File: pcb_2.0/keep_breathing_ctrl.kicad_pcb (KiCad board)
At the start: 4 copper layers, 153 x 148 mm, 260 parts, among them J1 Conn_02x04_Odd_Even, J2 1757284, J3 Conn_02x11_Odd_Even, P1 CONN_RASPBERRY, P2 Conn_01x04_Female, Q1 PN2222, Q2 PN2222, Q3 DMG2305UX, Q4 BCM857BS, Q5 2SC3325-Y, Q6 PN2222, Q7 PN2222, SW1 SW_DIP_x01, U1 MPL3115A2, U10 PCF8523TK, U11 AQH3223AX, U12 AQH3223AX, U13 HTS221, U14 ICE40UP5K-SG48ITR, U15 GD25Q32CTIGR-Memory_Flash, U16 UCC12040, U17 ISO7762, U18 XCL206B123, U19 AQH3223AX, U2 powerSTEP01, U20 AQH3223AX, U3 TLP240D, U4 TLP240D, U5 TLP240D, U6 TLP240D, U7 TLP240D, U8 TLP240D, U9 XCL214B333, X1 ABM8G, Y1 ABS06-107-32.768KHZ-T

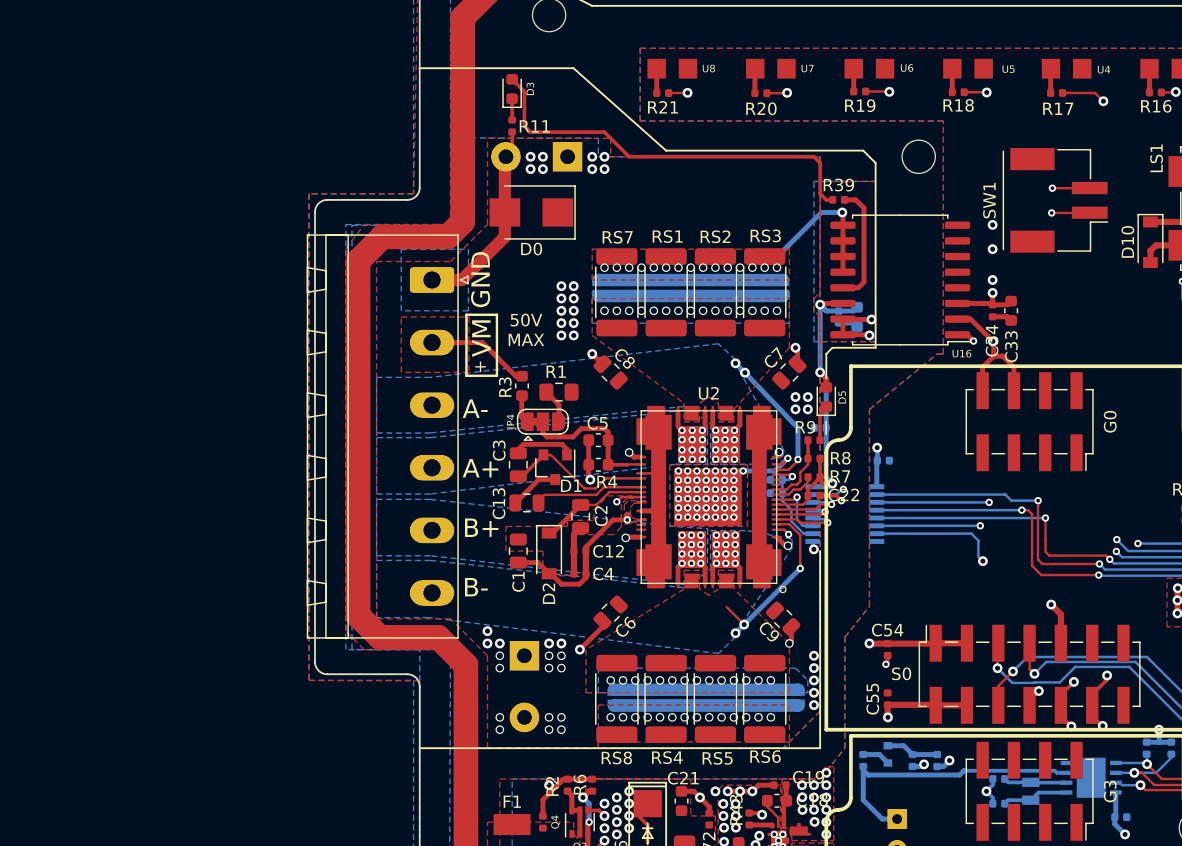
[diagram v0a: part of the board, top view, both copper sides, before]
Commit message: driver for motor eliminated
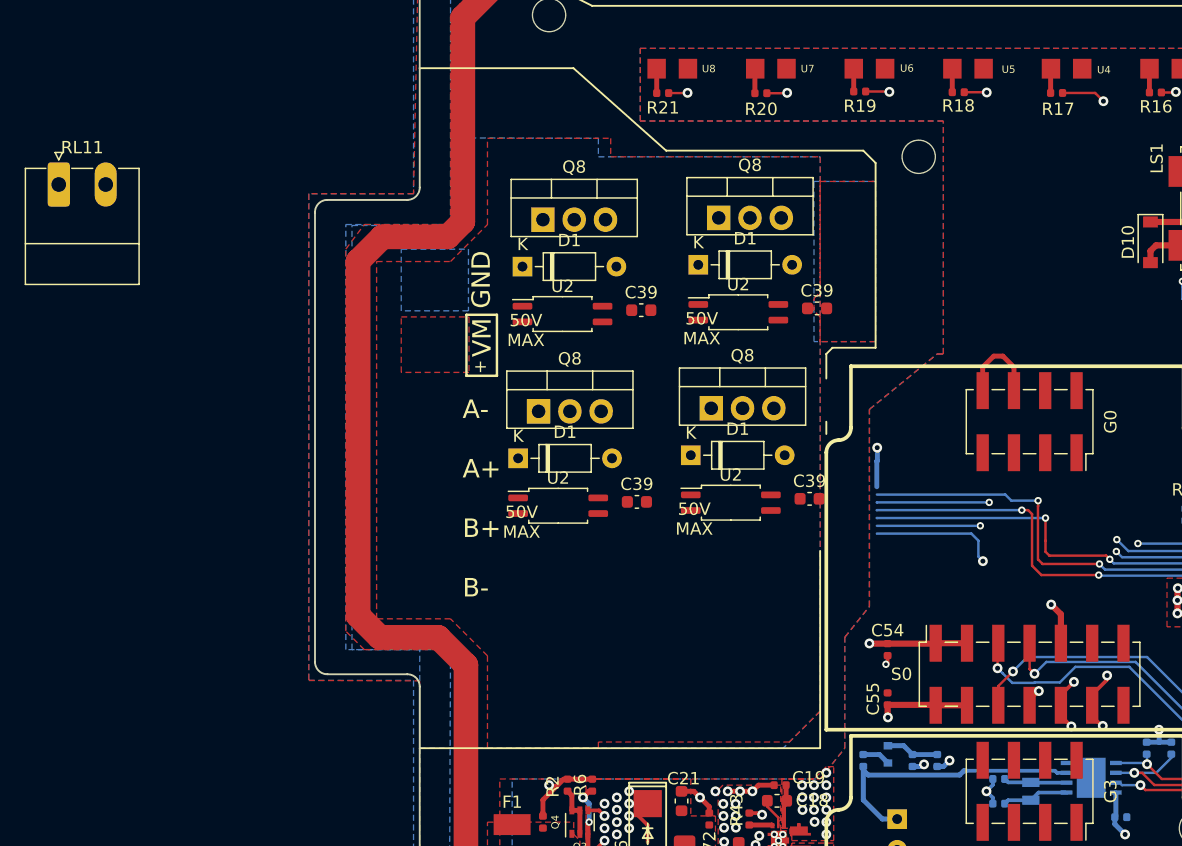
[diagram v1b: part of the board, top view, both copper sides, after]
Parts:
- removed C1: 22uF, Capacitor_SMD:C_0805_2012Metric
- removed C10, C11: 100uF 100V (Low ESR), Capacitor_THT:CP_Radial_D12.5mm_P5.00mm
- removed C12, C14, C22, C34, C35, C37, C74: 0.1uF, Capacitor_SMD:C_0402_1005Metric
- removed C13: 47nF 100V, Capacitor_SMD:C_0805_2012Metric
- removed C2, C3: 470nF 100V, Capacitor_SMD:C_0805_2012Metric
- removed C33, C36: 10uF, Capacitor_SMD:C_0603_1608Metric
- removed C4: 220nF, Capacitor_SMD:C_0402_1005Metric
- removed C5: 0.1uF, Capacitor_SMD:C_0603_1608Metric
- removed C6, C7, C8, C9: 220nF 100V, Capacitor_SMD:C_0805_2012Metric
- removed D0: 80V (Back EMF Clamp), Diode_SMD:D_SMB
- removed the D1 at (59.5, 87.7)
- removed D2: D_Schottky, Diode_SMD:D_SOD-123
- removed D3: LED GRN, Diode_SMD:D_0603_1608Metric
- removed D5: LED RED, Diode_SMD:D_0603_1608Metric
- removed J2: 1757284, Connector_Phoenix_MSTB:PhoenixContact_MSTBA_2,5_6-G-5,08_1x06_P5.08mm_Horizontal
- removed JP1, JP2: Jumper_2_Open, Klofas-Connectors:STpowerSTEP01_JMP
- removed JP4: SolderJumper_3_Bridged12, Jumper:SolderJumper-3_P1.3mm_Bridged12_RoundedPad1.0x1.5mm
- removed R1: -, Klofas-Passives:Resistor_NP_0805
- removed R11, R9: 330, Resistor_SMD:R_0402_1005Metric
- removed R3: 47K, Resistor_SMD:R_0603_1608Metric
- removed R39: 100k, Resistor_SMD:R_0402_1005Metric
- removed R4: 1.8K, Resistor_SMD:R_0603_1608Metric
- removed R63: 10k, Resistor_SMD:R_0402_1005Metric
- removed R7, R8: 39K, Resistor_SMD:R_0402_1005Metric
- removed RS1, RS2, RS3, RS4, RS5, RS6, RS7, RS8: 0.27, Resistor_SMD:R_2512_6332Metric
- removed SW1: SW_DIP_x01, Connector_Molex:Molex_CLIK-Mate_502443-0270_1x02-1MP_P2.00mm_Vertical
- removed U16: UCC12040, Package_SO:SOIC-16W_7.5x10.3mm_P1.27mm
- removed U17: ISO7762, Package_SO:SSOP-16_3.9x4.9mm_P0.635mm
- removed the U2 at (72.0, 90.1)
- added C39: 1uF, Capacitor_SMD:C_0603_1608Metric, F.Cu at (80.1, 90.3)
- added C39: 1uF, Capacitor_SMD:C_0603_1608Metric, F.Cu at (66.1, 90.5)
- added C39: 1uF, Capacitor_SMD:C_0603_1608Metric, F.Cu at (80.7, 74.8)
- added C39: 1uF, Capacitor_SMD:C_0603_1608Metric, F.Cu at (66.5, 75.0)
- added D1: 1N4148, Diode_THT:D_DO-35_SOD27_P7.62mm_Horizontal, F.Cu at (70.5, 86.7)
- added D1: 1N4148, Diode_THT:D_DO-35_SOD27_P7.62mm_Horizontal, F.Cu at (56.5, 87.0)
- added D1: 1N4148, Diode_THT:D_DO-35_SOD27_P7.62mm_Horizontal, F.Cu at (71.1, 71.3)
- added D1: 1N4148, Diode_THT:D_DO-35_SOD27_P7.62mm_Horizontal, F.Cu at (56.8, 71.4)
- added Q8: IRF540N, Package_TO_SOT_THT:TO-220-3_Vertical, F.Cu at (72.2, 82.9)
- added Q8: IRF540N, Package_TO_SOT_THT:TO-220-3_Vertical, F.Cu at (58.1, 83.2)
- added Q8: IRF540N, Package_TO_SOT_THT:TO-220-3_Vertical, F.Cu at (72.8, 67.5)
- added Q8: IRF540N, Package_TO_SOT_THT:TO-220-3_Vertical, F.Cu at (58.5, 67.6)
- added RL11: Conn_01x04_Female, Connector_Phoenix_MC:PhoenixContact_MC_1,5_2-G-3.81_1x02_P3.81mm_Horizontal, F.Cu at (19.2, 64.8)
- added U2: TLP291, Package_SO:SOIC-4_4.55x2.6mm_P1.27mm, F.Cu at (73.8, 90.6)
- added U2: TLP291, Package_SO:SOIC-4_4.55x2.6mm_P1.27mm, F.Cu at (59.7, 90.8)
- added U2: TLP291, Package_SO:SOIC-4_4.55x2.6mm_P1.27mm, F.Cu at (74.4, 75.1)
- added U2: TLP291, Package_SO:SOIC-4_4.55x2.6mm_P1.27mm, F.Cu at (60.1, 75.3)
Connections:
- UST1 pad 1: /Power Stepper/M_CLK -> /STM32F4/SPI4_SCK
- UST1 pad 2: /Power Stepper/M_RST -> /STM32F4/SPI4_RST
- UST1 pad 3: /Power Stepper/M_CS -> /STM32F4/SPI4_NSS
- UST1 pad 4: /Power Stepper/M_MISO -> /STM32F4/SPI4_MISO
- UST1 pad 5: /Power Stepper/M_MOSI -> /STM32F4/SPI4_MOSI
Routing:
- net 3V3_M: track 97.0 -> 0.00 mm, vias 4 -> 0
- net GND_MOTOR: track 70.1 -> 0.00 mm, vias 93 -> 0
- net /Power Stepper/SM_RST: track 49.2 -> 0.00 mm, vias 2 -> 0
- net Net-(SW1-Pad1): track 40.2 -> 0.00 mm, vias 2 -> 0
- net /STM32F4/SPI4_RST: track 0.00 -> 38.6 mm, vias 0 -> 2
- net /Power Stepper/M_RST: track 38.6 -> 0.00 mm, vias 2 -> 0
- net /STM32F4/SPI4_SCK: track 0.00 -> 37.9 mm, vias 0 -> 2
- net /Power Stepper/M_CLK: track 37.9 -> 0.00 mm, vias 2 -> 0
- net VMOTOR: track 37.1 -> 0.00 mm, vias 36 -> 0
- net /STM32F4/SPI4_NSS: track 0.00 -> 36.4 mm, vias 0 -> 2
- net /Power Stepper/M_CS: track 36.4 -> 0.00 mm, vias 2 -> 0
- net /STM32F4/SPI4_MOSI: track 0.00 -> 36.2 mm, vias 0 -> 2
- net /Power Stepper/M_MOSI: track 36.2 -> 0.00 mm, vias 2 -> 0
- net /STM32F4/SPI4_MISO: track 0.00 -> 34.9 mm, vias 0 -> 2
- net /Power Stepper/M_MISO: track 34.9 -> 0.00 mm, vias 2 -> 0
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- removed copper zone on B.Cu, net /Power Stepper/SENSEA_P
- removed copper zone on F.Cu, net /Power Stepper/SENSEA_P
- removed copper zone on B.Cu, net /Power Stepper/SENSEB_P
- removed copper zone on F.Cu, net /Power Stepper/SENSEB_P
- removed copper zone on F.Cu, net GND_MOTOR
- removed copper zone on B.Cu, net OUTA1
- removed copper zone on In2.Cu, net OUTA1
- removed copper zone on B.Cu, net OUTA2
- removed copper zone on In2.Cu, net OUTA2
- removed copper zone on B.Cu, net OUTB1
- removed copper zone on In2.Cu, net OUTB1
- removed copper zone on B.Cu, net OUTB2
- removed copper zone on In2.Cu, net OUTB2
